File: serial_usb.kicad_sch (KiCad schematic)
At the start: 24 parts, among them J2 3V3 Serial, J3 USB_C_USB2.0_16P, U17 ST16C550, U18 CP2102N, U23 74AHC1GU04, Y2 7.3728MHz

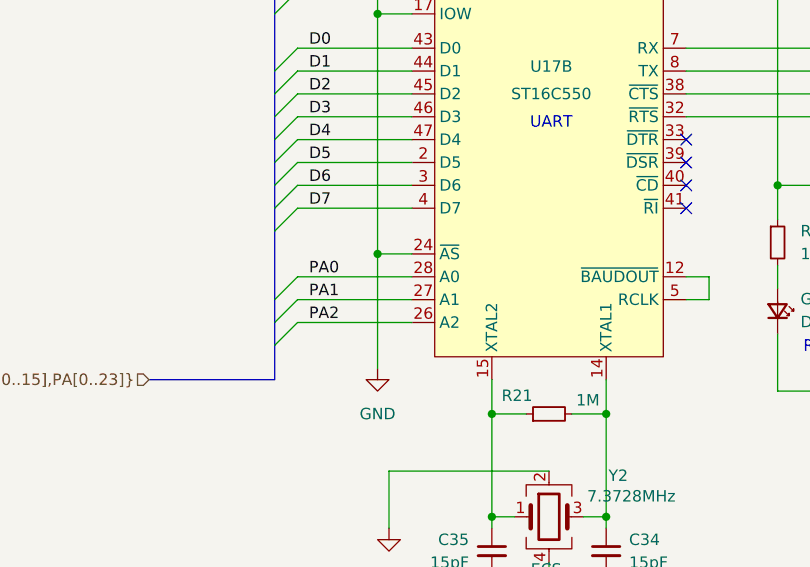
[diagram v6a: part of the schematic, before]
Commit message: fix UART addressing, generate gerbers
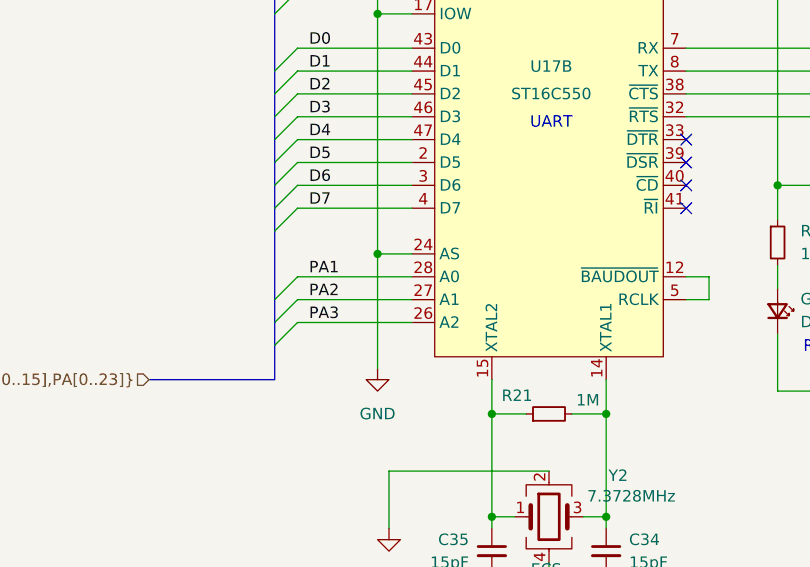
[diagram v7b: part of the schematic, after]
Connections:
- net PA0 is gone; now on net PA1: U17.28 (A0)
- net PA1: no longer U17.27 (A1)
- net PA2: now also U17.27 (A1); no longer U17.26 (A2)
- new net PA3: U17.26 (A2)
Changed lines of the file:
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@@
+		)
+	)
+	(label "PA3"
+		(at 138.43 175.26 0)
+		(fields_autoplaced yes)
+		(effects
+			(font
+				(size 1.27 1.27)
+			)
+			(justify left bottom)
 		)
 	)
 	(label "PA2"
-		(at 138.43 175.26 0)
-		(fields_autoplaced yes)
-		(effects
-			(font
-				(size 1.27 1.27)
-			)
-			(justify left bottom)
-		)
-	)
-	(label "PA1"
 		(at 138.43 172.72 0)
 		(fields_autoplaced yes)
@@
 		)
 	)
-	(label "PA0"
+	(label "PA1"
 		(at 138.43 170.18 0)
 		(fields_autoplaced yes)
@@
 	)
 	(symbol
+		(lib_name "ST16C550_1")
 		(lib_id "ST16C550:ST16C550")
 		(at 163.83 151.13 0)
